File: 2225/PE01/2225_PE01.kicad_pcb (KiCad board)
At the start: 2 copper layers, 200 x 60 mm, 95 parts

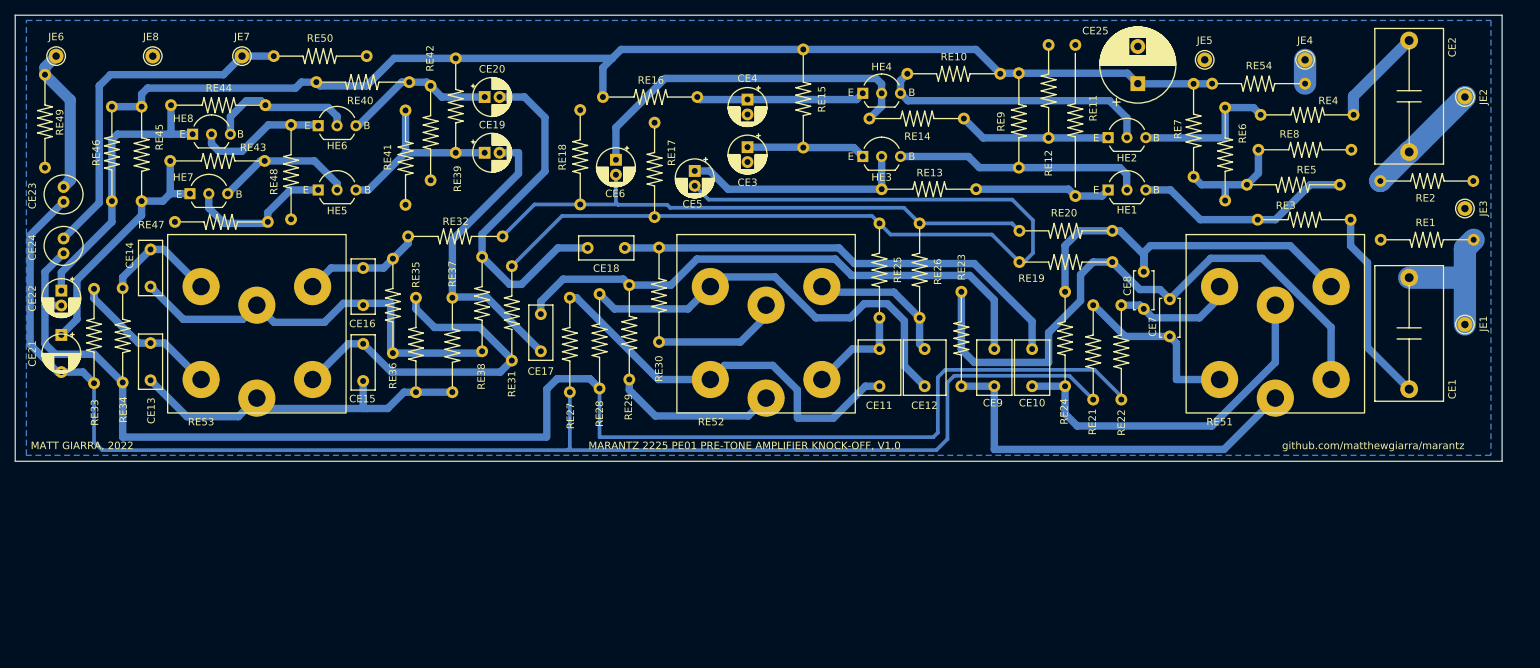
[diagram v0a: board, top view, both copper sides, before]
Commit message: Spaced out some components
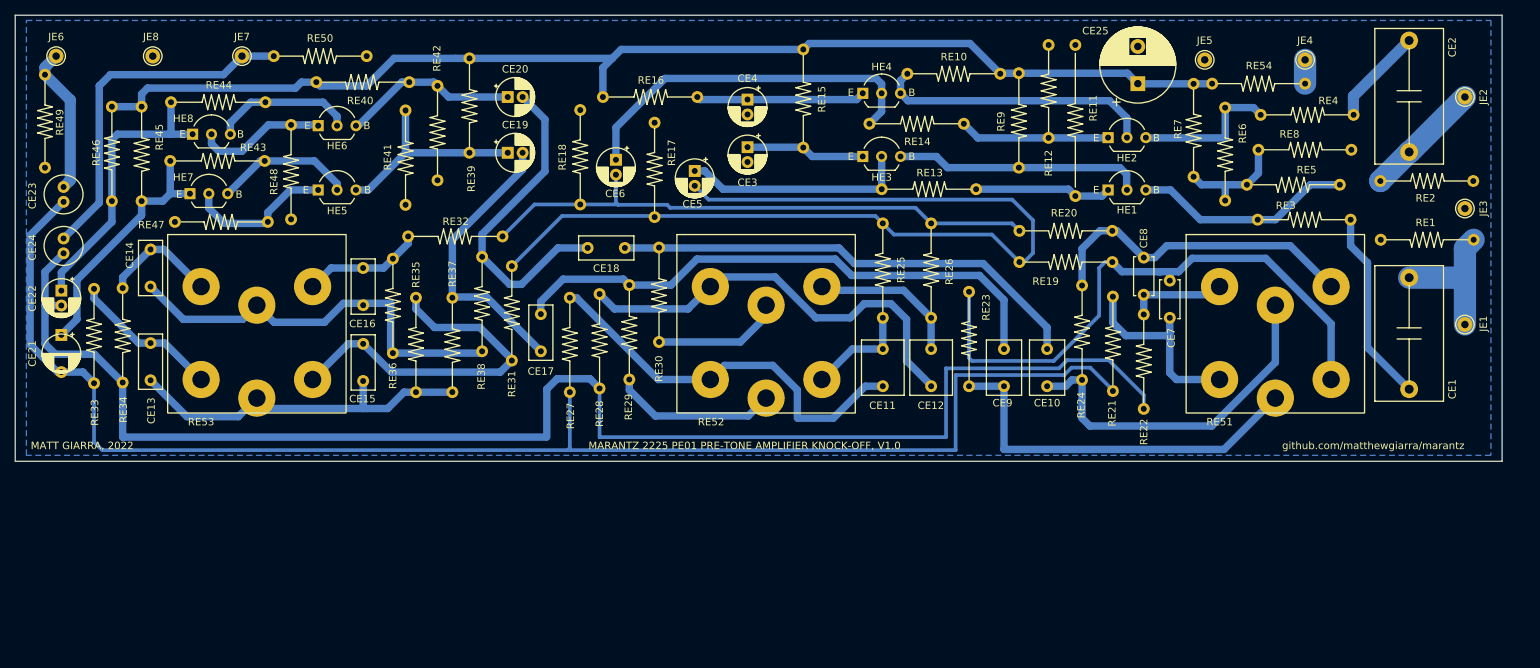
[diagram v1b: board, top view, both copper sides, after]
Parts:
- moved RE22 3.27 mm to (151.8, 40.2)
- moved CE19 3.10 mm to (66.2, 18.5)
- moved CE20 3.10 mm to (66.2, 11.0)
- moved RE21 2.89 mm to (147.7, 37.9)
- moved CE7 2.50 mm to (155.3, 40.7)
- moved RE24 2.44 mm to (143.5, 36.4)
- moved CE10 2.02 mm to (138.8, 49.9)
- moved CE8 1.90 mm to (151.8, 37.6)
- moved RE39 1.85 mm to (61.1, 18.5)
- moved RE26 1.55 mm to (123.2, 28.0)
- moved CE9 1.30 mm to (133.0, 49.9)
- moved RE23 1.03 mm to (128.3, 37.2)
- moved RE42 0.92 mm to (56.8, 9.50)
- moved CE12 0.87 mm to (123.2, 49.9)
- moved RE14 0.70 mm to (127.6, 14.6)
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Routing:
- net Net-(RE51-Pad4): track 51.7 -> 43.9 mm
- net Net-(CE22-Pad2): track 193.9 -> 200.2 mm
- net Net-(CE21-Pad2): track 192.5 -> 197.0 mm
- net Net-(CE18-Pad2): track 47.3 -> 44.0 mm
- net Net-(RE51-Pad6): track 16.5 -> 13.3 mm
- net Net-(CE20-Pad1): track 20.6 -> 23.7 mm
- net Net-(CE19-Pad1): track 25.1 -> 28.2 mm
- net Net-(RE51-Pad1): track 23.9 -> 26.5 mm
- net Net-(RE51-Pad3): track 83.4 -> 81.0 mm
- net Net-(CE17-Pad2): track 40.7 -> 38.4 mm
- net Net-(CE10-Pad2): track 62.4 -> 63.9 mm
- net Net-(CE17-Pad1): track 74.6 -> 75.9 mm
- net Net-(RE52-Pad4): track 19.4 -> 20.6 mm
- net Net-(RE51-Pad2): track 53.6 -> 52.6 mm
- net Net-(CE6-Pad1): track 48.5 -> 49.2 mm
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
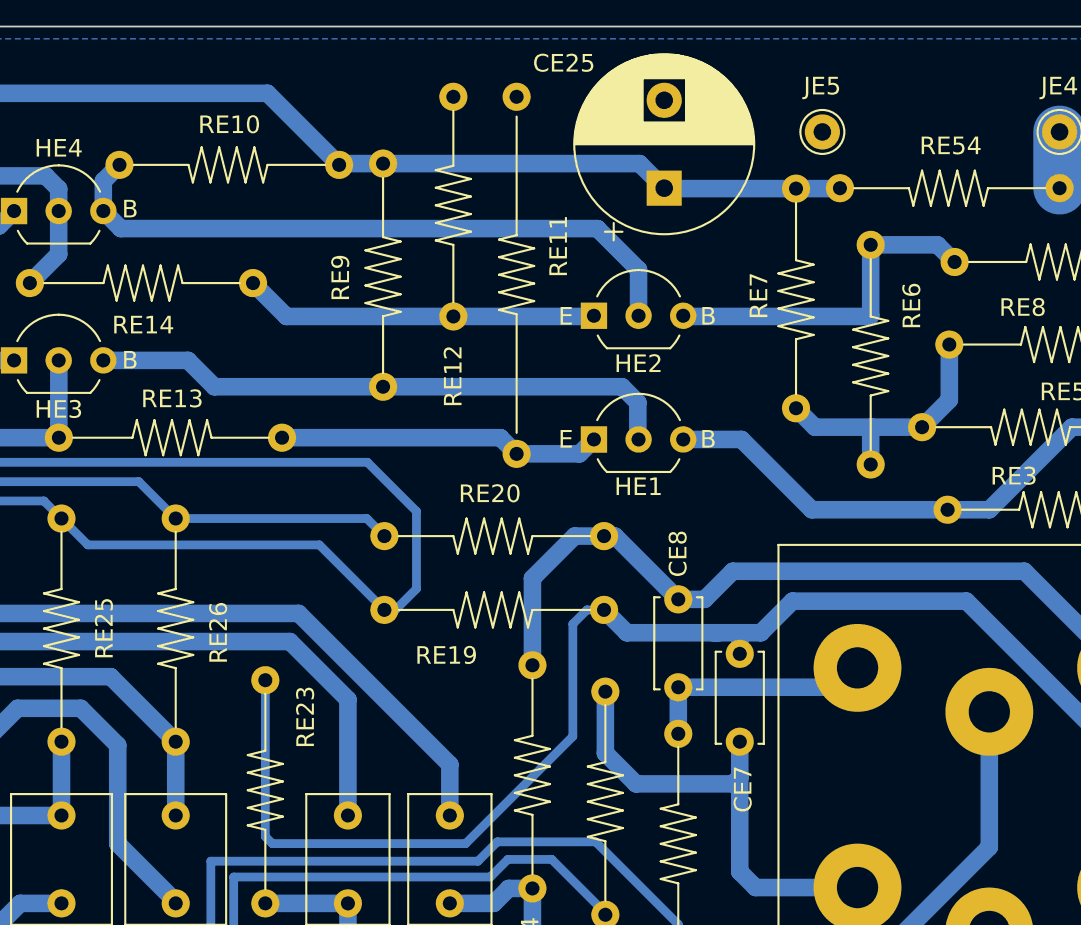
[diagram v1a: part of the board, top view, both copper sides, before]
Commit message: Minor trace moves
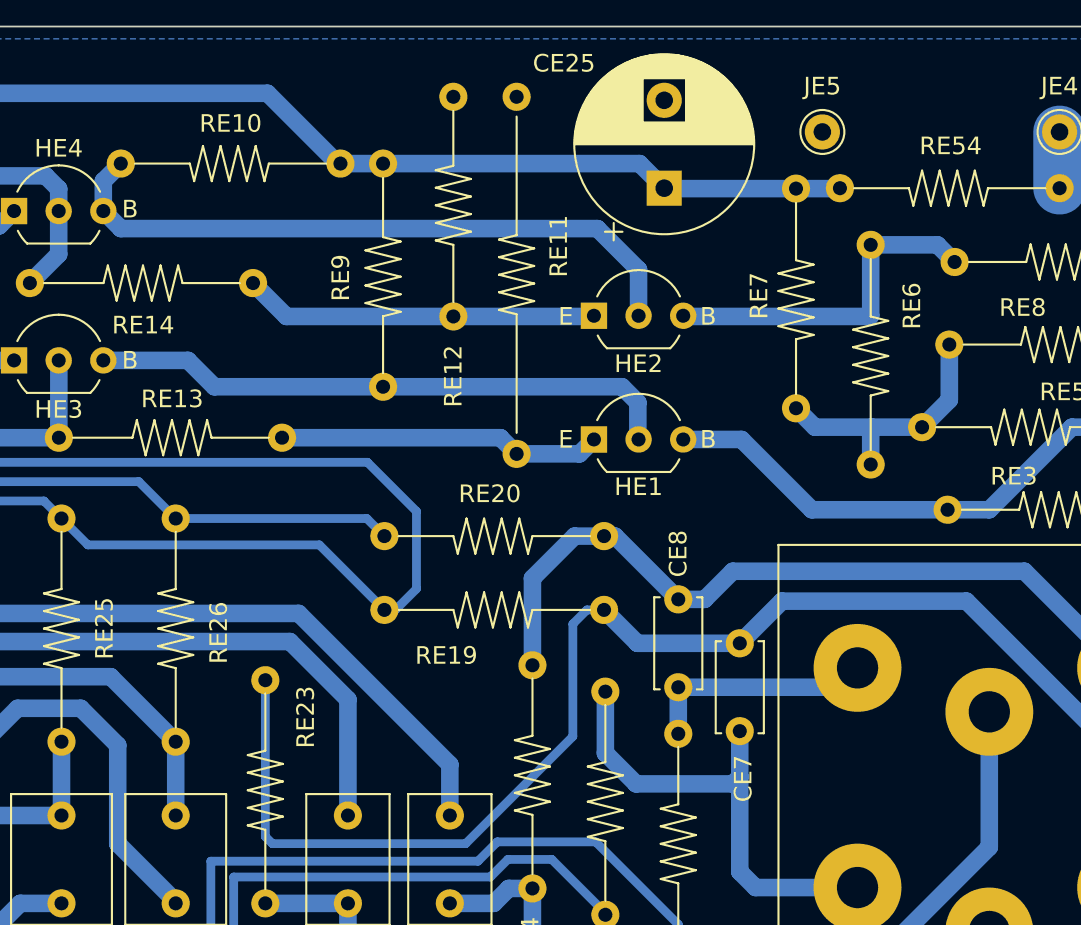
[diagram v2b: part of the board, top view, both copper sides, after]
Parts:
- moved CE7 0.60 mm to (155.3, 40.1)
- moved RE10 0.11 mm to (120.1, 7.80)
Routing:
- net Net-(RE51-Pad3): track 81.0 -> 79.9 mm
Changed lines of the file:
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@@
   )
   (footprint "Resistor_THT:R_US_Axial_DIN0309_L9.0mm_D3.2mm_P12.50mm_Horizontal" (layer "F.Cu")
-    (at 120 7.874)
+    (at 120.075 7.8)
     (descr "Resistor, Axial_DIN0309 series, Axial, Horizontal, pin pitch=12.7mm, 0.5W = 1/2W, length*diameter=9*3.2mm^2, http://cdn-reichelt.de/documents/datenblatt/B400/1_4W%23YAG.pdf")
     (tags "Resistor Axial_DIN0309 series Axial Horizontal pin pitch 12.7mm 0.5W = 1/2W length 9mm diameter 3.2mm")
@@
   )
   (footprint "Capacitor_THT:C_Disc_D5.0mm_W2.5mm_P5.00mm" (layer "F.Cu")
-    (at 155.3 40.7 90)
+    (at 155.3 40.1 90)
     (descr "C, Disc series, Radial, pin pitch=5.00mm, , diameter*width=5*2.5mm^2, Capacitor, http://cdn-reichelt.de/documents/datenblatt/B300/DS_KERKO_TC.pdf")
     (tags "C Disc series Radial pin pitch 5.00mm  diameter 5mm width 2.5mm Capacitor")
@@
   (segment (start 165.675 22.8) (end 162.8 22.8) (width 1) (layer "B.Cu") (net 34))
   (segment (start 162.8 22.8) (end 162.75 22.85) (width 1) (layer "B.Cu") (net 34))
+  (segment (start 157.7 32.7) (end 168.2 32.7) (width 1) (layer "B.Cu") (net 36))
+  (segment (start 155.3 35.1) (end 157.7 32.7) (width 1) (layer "B.Cu") (net 36))
   (segment (start 145.8 34) (end 145.8 40.4) (width 0.5) (layer "B.Cu") (net 36))
-  (segment (start 155.3 34.7) (end 155.1 34.5) (width 1) (layer "B.Cu") (net 36))
-  (segment (start 168.2 32.7) (end 177 41.5) (width 1) (layer "B.Cu") (net 36))
+  (segment (start 155.3 35.1) (end 149.475 35.1) (width 1) (layer "B.Cu") (net 36))
+  (segment (start 149.475 35.1) (end 147.575 33.2) (width 1) (layer "B.Cu") (net 36))
   (segment (start 177 41.5) (end 177 49) (width 1) (layer "B.Cu") (net 36))
   (segment (start 128.7 46.5) (end 128.3 46.1) (width 0.5) (layer "B.Cu") (net 36))
-  (segment (start 148.875 34.5) (end 147.575 33.2) (width 1) (layer "B.Cu") (net 36))
   (segment (start 139.7 46.5) (end 128.7 46.5) (width 0.5) (layer "B.Cu") (net 36))
   (segment (start 128.3 46.1) (end 128.3 37.2) (width 0.5) (layer "B.Cu") (net 36))
-  (segment (start 155.3 35.7) (end 155.3 34.7) (width 1) (layer "B.Cu") (net 36))
-  (segment (start 156.5 34.5) (end 158.3 32.7) (width 1) (layer "B.Cu") (net 36))
   (segment (start 146.6 33.2) (end 145.8 34) (width 0.5) (layer "B.Cu") (net 36))
   (segment (start 147.575 33.2) (end 146.6 33.2) (width 0.5) (layer "B.Cu") (net 36))
   (segment (start 145.8 40.4) (end 139.7 46.5) (width 0.5) (layer "B.Cu") (net 36))
-  (segment (start 158.3 32.7) (end 168.2 32.7) (width 1) (layer "B.Cu") (net 36))
-  (segment (start 153.8 34.5) (end 155.1 34.5) (width 1) (layer "B.Cu") (net 36))
-  (segment (start 155.1 34.5) (end 156.5 34.5) (width 1) (layer "B.Cu") (net 36))
-  (segment (start 154.1 34.5) (end 148.875 34.5) (width 1) (layer "B.Cu") (net 36))
+  (segment (start 168.2 32.7) (end 177 41.5) (width 1) (layer "B.Cu") (net 36))
   (segment (start 147.65 37.85) (end 147.65 41.35) (width 1) (layer "B.Cu") (net 37))
   (segment (start 155.3 48.1) (end 156.2 49) (width 1) (layer "B.Cu") (net 37))
@@
   (segment (start 145.9 29) (end 143.5 31.4) (width 1) (layer "B.Cu") (net 38))
   (segment (start 147.575 29) (end 145.9 29) (width 1) (layer "B.Cu") (net 38))
-  (segment (start 151.8 37.6) (end 151.8 40.25) (width 1) (layer "B.Cu") (net 39))
   (segment (start 151.8 37.6) (end 160.9 37.6) (width 1) (layer "B.Cu") (net 39))
+  (segment (start 151.8 37.6) (end 151.8 40.25) (width 1) (layer "B.Cu") (net 39))
   (segment (start 160.9 37.6) (end 162 36.5) (width 1) (layer "B.Cu") (net 39))
   (segment (start 133 58.4) (end 162.6 58.4) (width 1) (layer "B.Cu") (net 40))

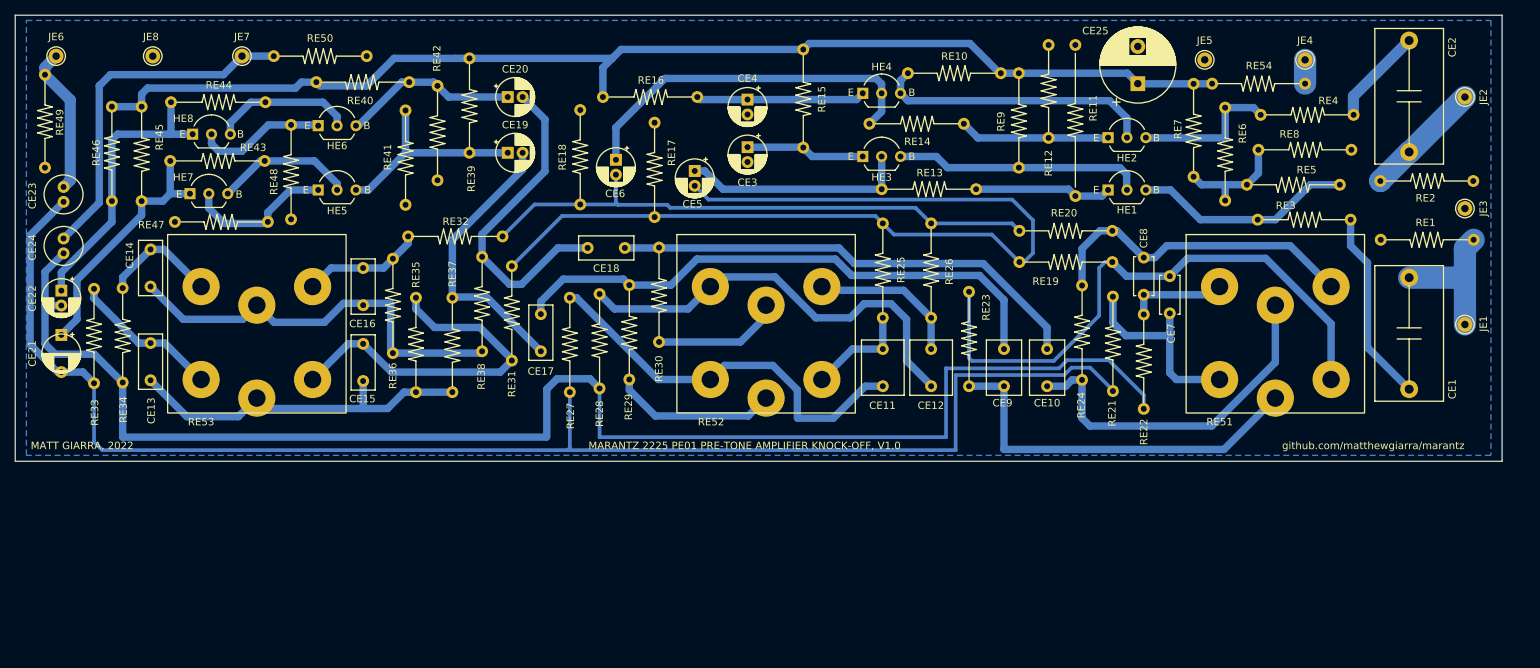
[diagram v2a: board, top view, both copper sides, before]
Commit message: Updated footprints of resitors and caps to match final component selections
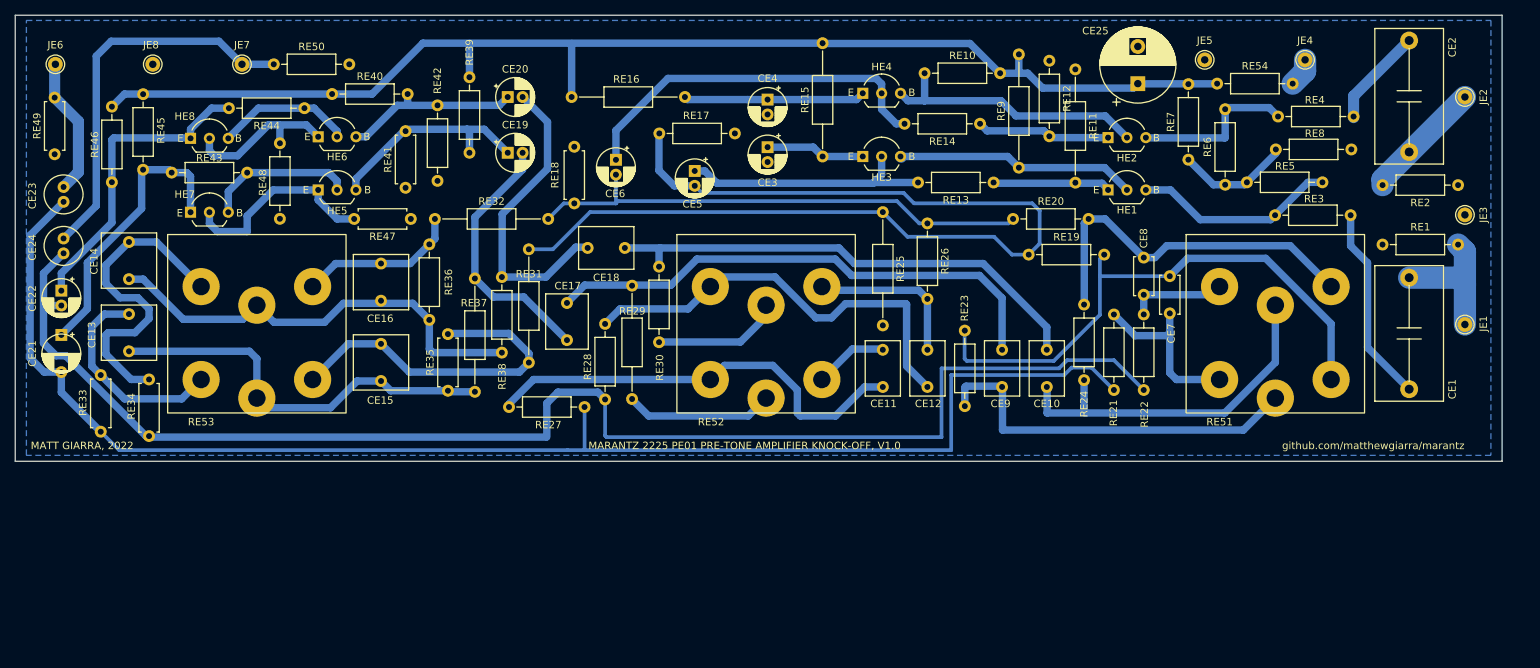
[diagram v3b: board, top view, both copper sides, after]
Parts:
- CE11, CE12: footprint Capacitor_THT:C_Rect_L7.2mm_W5.5mm_P5.00mm_FKS2_FKP2_MKS2_MKP2 -> Capacitor_THT:C_Rect_L7.2mm_W4.5mm_P5.00mm_FKS2_FKP2_MKS2_MKP2
- CE13, CE14, CE15, CE16: footprint Capacitor_THT:C_Rect_L7.2mm_W3.0mm_P5.00mm_FKS2_FKP2_MKS2_MKP2 -> Capacitor_THT:C_Rect_L7.2mm_W7.2mm_P5.00mm_FKS2_FKP2_MKS2_MKP2
- CE17, CE18: footprint Capacitor_THT:C_Rect_L7.2mm_W3.0mm_P5.00mm_FKS2_FKP2_MKS2_MKP2 -> Capacitor_THT:C_Rect_L7.2mm_W5.5mm_P5.00mm_FKS2_FKP2_MKS2_MKP2
- RE1, RE10, RE12, RE19, RE2, RE20, RE3, RE4, RE40, RE5, RE50, RE54, RE6, RE7, RE8: footprint Resistor_THT:R_US_Axial_DIN0309_L9.0mm_D3.2mm_P12.50mm_Horizontal -> Resistor_THT:R_Axial_DIN0207_L6.3mm_D2.5mm_P10.16mm_Horizontal
- RE11: footprint Resistor_THT:R_US_Axial_DIN0309_L9.0mm_D3.2mm_P20.32mm_Horizontal -> Resistor_THT:R_Axial_DIN0207_L6.3mm_D2.5mm_P15.24mm_Horizontal
- RE13, RE14, RE17, RE21, RE22, RE23, RE24, RE26, RE27, RE28, RE30, RE36, RE38, RE39, RE42, RE43, RE44, RE45, RE46, RE48: footprint Resistor_THT:R_US_Axial_DIN0309_L9.0mm_D3.2mm_P12.70mm_Horizontal -> Resistor_THT:R_Axial_DIN0207_L6.3mm_D2.5mm_P10.16mm_Horizontal
- RE15: footprint Resistor_THT:R_US_Axial_DIN0309_L9.0mm_D3.2mm_P13.20mm_Horizontal -> Resistor_THT:R_Axial_DIN0207_L6.3mm_D2.5mm_P15.24mm_Horizontal
- RE16, RE25, RE29, RE31, RE32, RE37, RE9: footprint Resistor_THT:R_US_Axial_DIN0309_L9.0mm_D3.2mm_P12.70mm_Horizontal -> Resistor_THT:R_Axial_DIN0207_L6.3mm_D2.5mm_P15.24mm_Horizontal
- RE18, RE33, RE34, RE35, RE41: footprint Resistor_THT:R_US_Axial_DIN0309_L9.0mm_D3.2mm_P12.70mm_Horizontal -> Resistor_THT:R_Axial_DIN0207_L6.3mm_D2.5mm_P7.62mm_Horizontal
- RE47, RE49: footprint Resistor_THT:R_US_Axial_DIN0309_L9.0mm_D3.2mm_P12.50mm_Horizontal -> Resistor_THT:R_Axial_DIN0207_L6.3mm_D2.5mm_P7.62mm_Horizontal
- moved RE47 31.7 mm to (53.2, 27.4), turned to 180 degrees
- moved RE27 16.8 mm to (66.4, 52.7), turned to 0 degrees
- moved RE33 11.6 mm to (11.5, 48.4)
- moved RE17 10.9 mm to (96.8, 15.9), turned to 180 degrees
- moved RE34 8.04 mm to (18.0, 56.6)
- moved RE35 6.51 mm to (58.2, 42.9)
- moved RE44 5.31 mm to (38.9, 12.5)
- moved RE36 5.27 mm to (55.7, 30.8)
- moved RE23 5.25 mm to (127.7, 42.4)
- moved RE18 5.00 mm to (75.2, 17.7)
- moved CE13 4.86 mm to (15.3, 40.2)
- moved RE32 4.30 mm to (56.5, 27.4)
- moved RE45 4.22 mm to (17.2, 20.8)
- moved RE28 4.09 mm to (79.3, 41.5)
- moved CE17 3.82 mm to (74.2, 38.7)
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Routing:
- net Net-(RE53-Pad6): track 15.6 -> 44.1 mm
- net Net-(CE22-Pad2): track 200.2 -> 190.5 mm
- net Net-(CE25-Pad1): track 160.9 -> 169.3 mm
- net Net-(RE53-Pad1): track 20.2 -> 28.6 mm
- net Net-(CE5-Pad2): track 128.3 -> 136.6 mm
- net Net-(CE6-Pad2): track 76.9 -> 68.7 mm
- net Net-(HE5-Pad1): track 20.1 -> 27.4 mm
- net Net-(RE53-Pad2): track 48.9 -> 54.9 mm
- net Net-(CE17-Pad1): track 75.9 -> 70.1 mm
- net Net-(RE51-Pad4): track 43.9 -> 49.5 mm
- net Net-(RE53-Pad4): track 16.2 -> 21.8 mm
- net Net-(RE52-Pad1): track 54.3 -> 59.1 mm
- net Net-(CE24-Pad2): track 47.6 -> 52.3 mm
- net Net-(CE21-Pad1): track 33.8 -> 38.3 mm
- net Net-(CE5-Pad1): track 30.6 -> 34.8 mm
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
